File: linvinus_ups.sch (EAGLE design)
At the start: 19 parts, among them J1 BATTERY_CONNDEANS, Q1 IRF7240PBF, Q2 IRF7240PBF, Q3 BSS123, Q4 IRF7240PBF

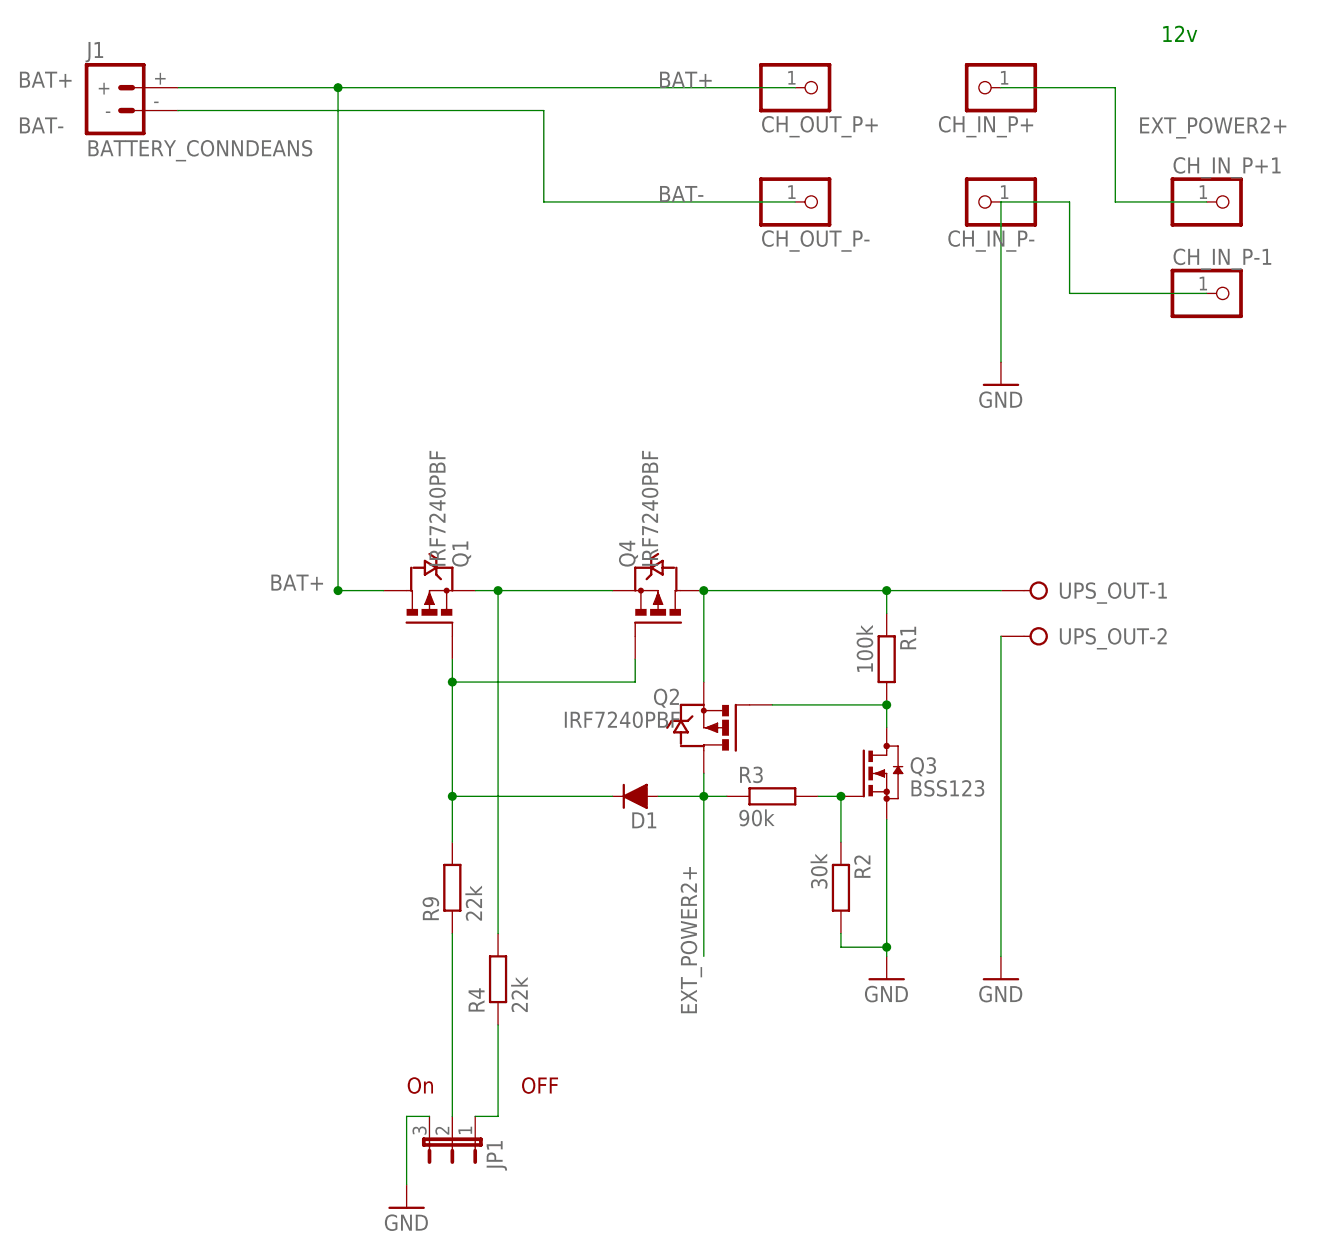
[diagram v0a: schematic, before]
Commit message: fix, completely close Q4 if vbatt > external power
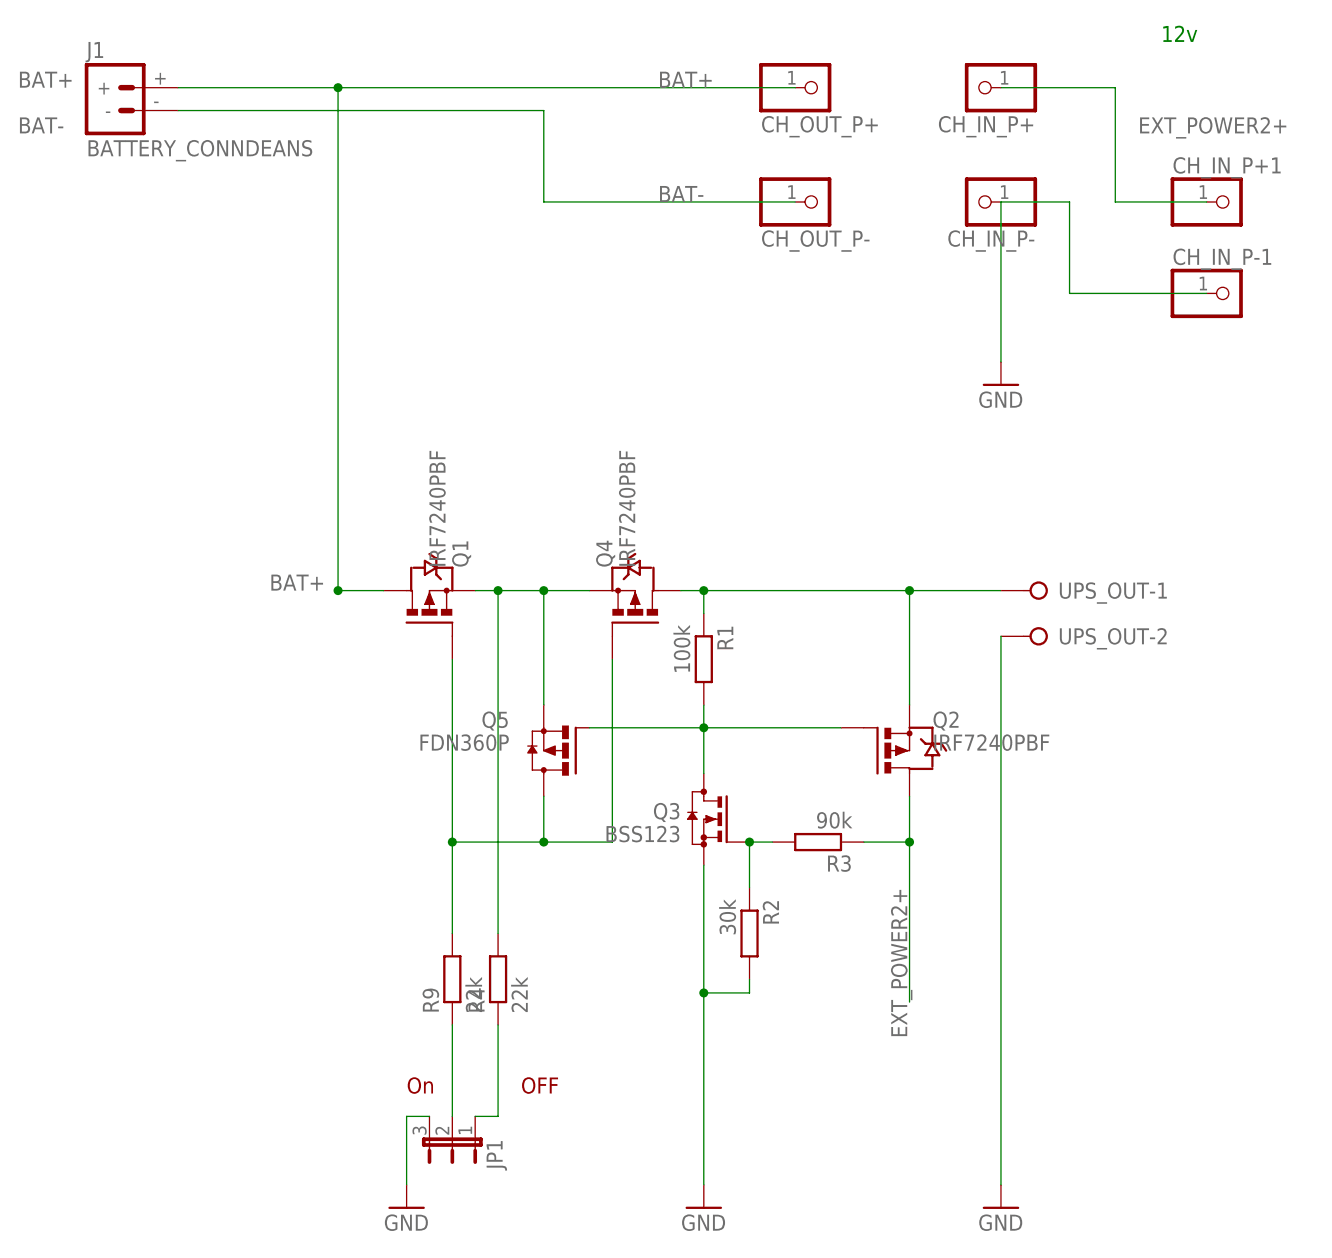
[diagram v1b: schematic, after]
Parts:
- removed D1: (no value), semicon-smd-ipc:D-FILL-SOD-80
- added Q5: FDN360P, transistor-power:FDN360P
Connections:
- net EXT_POWER2+: no longer D1.A
- net N$1: now also Q5.G
- net N$10: now also Q5.D; no longer D1.C
- net N$5: now also Q5.S
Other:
- moved on the sheet: Q2, Q3, Q4, R1, R2, R3, R9
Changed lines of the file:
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@@
 <part name="CH_IN_P-1" library="pinhead" deviceset="PINHD-1X1" device=""/>
 <part name="Q4" library="transistor-power" deviceset="P-MOSFET-SO8" device="" value="IRF7240PBF"/>
-<part name="D1" library="semicon-smd-ipc" deviceset="D-FILL-" device="SOD-80"/>
 <part name="R4" library="resistor" deviceset="R-EU_" device="R0805" value="22k"/>
 <part name="JP1" library="jumper" deviceset="JP2E" device=""/>
+<part name="Q5" library="transistor-power" deviceset="FDN360P" device=""/>
 </parts>
 <sheets>
@@
 <instance part="GND1" gate="1" x="124.46" y="66.04"/>
 <instance part="GND3" gate="1" x="58.42" y="-25.4"/>
-<instance part="R9" gate="G$1" x="63.5" y="10.16" rot="R90"/>
-<instance part="GND7" gate="1" x="124.46" y="0"/>
-<instance part="Q2" gate="G$1" x="93.98" y="27.94" rot="MR0"/>
-<instance part="Q3" gate="G$1" x="111.76" y="22.86"/>
-<instance part="R1" gate="G$1" x="111.76" y="35.56" rot="R270"/>
-<instance part="R2" gate="G$1" x="106.68" y="10.16" rot="R270"/>
-<instance part="R3" gate="G$1" x="99.06" y="20.32"/>
-<instance part="GND2" gate="1" x="111.76" y="0"/>
+<instance part="R9" gate="G$1" x="63.5" y="0" rot="R90"/>
+<instance part="GND7" gate="1" x="124.46" y="-25.4"/>
+<instance part="Q2" gate="G$1" x="111.76" y="25.4"/>
+<instance part="Q3" gate="G$1" x="91.44" y="17.78" rot="MR0"/>
+<instance part="R1" gate="G$1" x="91.44" y="35.56" rot="R270"/>
+<instance part="R2" gate="G$1" x="96.52" y="5.08" rot="R270"/>
+<instance part="R3" gate="G$1" x="104.14" y="15.24" rot="R180"/>
+<instance part="GND2" gate="1" x="91.44" y="-25.4"/>
 <instance part="J1" gate="G$1" x="25.4" y="99.06"/>
 <instance part="CH_IN_P+1" gate="G$1" x="149.86" y="86.36"/>
 <instance part="CH_IN_P-1" gate="G$1" x="149.86" y="76.2"/>
-<instance part="Q4" gate="G$1" x="86.36" y="40.64" rot="R90"/>
-<instance part="D1" gate="G$1" x="83.82" y="20.32" rot="R180"/>
+<instance part="Q4" gate="G$1" x="83.82" y="40.64" rot="R90"/>
 <instance part="R4" gate="G$1" x="68.58" y="0" rot="R90"/>
 <instance part="JP1" gate="1" x="63.5" y="-17.78" rot="R180"/>
+<instance part="Q5" gate="G$1" x="76.2" y="25.4" rot="MR0"/>
 </instances>
 <busses>
@@
 <net name="EXT_POWER2+" class="0">
 <segment>
-<label x="88.9" y="12.7" size="1.778" layer="95" rot="R270"/>
-<wire x1="91.44" y1="20.32" x2="91.44" y2="2.54" width="0.1524" layer="91"/>
+<label x="112.268" y="10.16" size="1.778" layer="95" rot="R270"/>
+<wire x1="114.3" y1="20.32" x2="114.3" y2="15.24" width="0.1524" layer="91"/>
 <pinref part="Q2" gate="G$1" pin="D"/>
-<wire x1="91.44" y1="20.32" x2="91.44" y2="22.86" width="0.1524" layer="91"/>
-<junction x="91.44" y="20.32"/>
 <pinref part="R3" gate="G$1" pin="1"/>
-<wire x1="91.44" y1="20.32" x2="93.98" y2="20.32" width="0.1524" layer="91"/>
-<pinref part="D1" gate="G$1" pin="A"/>
-<wire x1="86.36" y1="20.32" x2="91.44" y2="20.32" width="0.1524" layer="91"/>
+<wire x1="114.3" y1="15.24" x2="114.3" y2="-2.54" width="0.1524" layer="91"/>
+<wire x1="109.22" y1="15.24" x2="114.3" y2="15.24" width="0.1524" layer="91"/>
+<junction x="114.3" y="15.24"/>
 </segment>
 <segment>
@@
 <segment>
 <pinref part="UPS_OUT" gate="-2" pin="KL"/>
-<wire x1="124.46" y1="38.1" x2="124.46" y2="2.54" width="0.1524" layer="91"/>
+<wire x1="124.46" y1="38.1" x2="124.46" y2="-22.86" width="0.1524" layer="91"/>
 <pinref part="GND7" gate="1" pin="GND"/>
 </segment>
@@
 <pinref part="Q3" gate="G$1" pin="S"/>
 <pinref part="GND2" gate="1" pin="GND"/>
-<wire x1="111.76" y1="17.78" x2="111.76" y2="4.064" width="0.1524" layer="91"/>
+<wire x1="91.44" y1="12.7" x2="91.44" y2="-1.524" width="0.1524" layer="91"/>
 <pinref part="R2" gate="G$1" pin="2"/>
-<wire x1="111.76" y1="3.556" x2="111.76" y2="2.54" width="0.1524" layer="91"/>
-<wire x1="106.68" y1="5.08" x2="106.68" y2="3.556" width="0.1524" layer="91"/>
-<wire x1="106.68" y1="3.556" x2="111.76" y2="3.556" width="0.1524" layer="91"/>
-<wire x1="111.76" y1="3.556" x2="111.76" y2="4.064" width="0.1524" layer="91"/>
-<junction x="111.76" y="3.556"/>
+<wire x1="91.44" y1="-1.524" x2="91.44" y2="-22.86" width="0.1524" layer="91"/>
+<wire x1="96.52" y1="0" x2="96.52" y2="-1.524" width="0.1524" layer="91"/>
+<wire x1="96.52" y1="-1.524" x2="91.44" y2="-1.524" width="0.1524" layer="91"/>
+<junction x="91.44" y="-1.524"/>
 </segment>
 <segment>
@@
 </segment>
 </net>
-<net name="N$6" class="0">
-<segment>
-<pinref part="UPS_OUT" gate="-1" pin="KL"/>
-<wire x1="124.46" y1="43.18" x2="111.76" y2="43.18" width="0.1524" layer="91"/>
-<pinref part="Q2" gate="G$1" pin="S"/>
-<wire x1="111.76" y1="43.18" x2="91.44" y2="43.18" width="0.1524" layer="91"/>
-<wire x1="91.44" y1="33.02" x2="91.44" y2="43.18" width="0.1524" layer="91"/>
-<pinref part="R1" gate="G$1" pin="1"/>
-<wire x1="111.76" y1="40.64" x2="111.76" y2="43.18" width="0.1524" layer="91"/>
-<junction x="111.76" y="43.18"/>
-<pinref part="Q4" gate="G$1" pin="D"/>
-<junction x="91.44" y="43.18"/>
-</segment>
-</net>
 <net name="N$10" class="0">
 <segment>
 <pinref part="Q1" gate="G$1" pin="G"/>
 <pinref part="R9" gate="G$1" pin="2"/>
-<wire x1="63.5" y1="15.24" x2="63.5" y2="20.32" width="0.1524" layer="91"/>
-<wire x1="63.5" y1="20.32" x2="63.5" y2="33.02" width="0.1524" layer="91"/>
-<wire x1="63.5" y1="33.02" x2="63.5" y2="35.56" width="0.1524" layer="91"/>
+<wire x1="63.5" y1="5.08" x2="63.5" y2="15.24" width="0.1524" layer="91"/>
+<wire x1="63.5" y1="15.24" x2="63.5" y2="35.56" width="0.1524" layer="91"/>
 <pinref part="Q4" gate="G$1" pin="G"/>
-<wire x1="83.82" y1="35.56" x2="83.82" y2="33.02" width="0.1524" layer="91"/>
-<wire x1="83.82" y1="33.02" x2="63.5" y2="33.02" width="0.1524" layer="91"/>
-<junction x="63.5" y="33.02"/>
-<pinref part="D1" gate="G$1" pin="C"/>
-<wire x1="81.28" y1="20.32" x2="63.5" y2="20.32" width="0.1524" layer="91"/>
-<junction x="63.5" y="20.32"/>
+<wire x1="81.28" y1="35.56" x2="81.28" y2="15.24" width="0.1524" layer="91"/>
+<wire x1="81.28" y1="15.24" x2="73.66" y2="15.24" width="0.1524" layer="91"/>
+<junction x="63.5" y="15.24"/>
+<wire x1="73.66" y1="15.24" x2="63.5" y2="15.24" width="0.1524" layer="91"/>
+<pinref part="Q5" gate="G$1" pin="D"/>
+<wire x1="73.66" y1="20.32" x2="73.66" y2="15.24" width="0.1524" layer="91"/>
+<junction x="73.66" y="15.24"/>
 </segment>
 </net>
@@
 <net name="N$1" class="0">
 <segment>
+<pinref part="R1" gate="G$1" pin="2"/>
+<pinref part="Q3" gate="G$1" pin="D"/>
+<wire x1="91.44" y1="30.48" x2="91.44" y2="27.94" width="0.1524" layer="91"/>
+<pinref part="Q5" gate="G$1" pin="G"/>
+<wire x1="91.44" y1="27.94" x2="91.44" y2="22.86" width="0.1524" layer="91"/>
+<wire x1="78.74" y1="27.94" x2="91.44" y2="27.94" width="0.1524" layer="91"/>
+<junction x="91.44" y="27.94"/>
 <pinref part="Q2" gate="G$1" pin="G"/>
-<pinref part="R1" gate="G$1" pin="2"/>
-<wire x1="99.06" y1="30.48" x2="111.76" y2="30.48" width="0.1524" layer="91"/>
-<pinref part="Q3" gate="G$1" pin="D"/>
-<wire x1="111.76" y1="30.48" x2="111.76" y2="27.94" width="0.1524" layer="91"/>
-<junction x="111.76" y="30.48"/>
+<wire x1="106.68" y1="27.94" x2="91.44" y2="27.94" width="0.1524" layer="91"/>
 </segment>
 </net>
@@
 <pinref part="R3" gate="G$1" pin="2"/>
 <pinref part="Q3" gate="G$1" pin="G"/>
-<wire x1="104.14" y1="20.32" x2="106.68" y2="20.32" width="0.1524" layer="91"/>
+<wire x1="99.06" y1="15.24" x2="96.52" y2="15.24" width="0.1524" layer="91"/>
 <pinref part="R2" gate="G$1" pin="1"/>
-<wire x1="106.68" y1="15.24" x2="106.68" y2="20.32" width="0.1524" layer="91"/>
-<junction x="106.68" y="20.32"/>
+<wire x1="96.52" y1="10.16" x2="96.52" y2="15.24" width="0.1524" layer="91"/>
+<junction x="96.52" y="15.24"/>
 </segment>
 </net>
@@
 <wire x1="66.04" y1="43.18" x2="68.58" y2="43.18" width="0.1524" layer="91"/>
 <pinref part="R4" gate="G$1" pin="2"/>
-<wire x1="68.58" y1="43.18" x2="81.28" y2="43.18" width="0.1524" layer="91"/>
+<wire x1="68.58" y1="43.18" x2="73.66" y2="43.18" width="0.1524" layer="91"/>
+<wire x1="73.66" y1="43.18" x2="78.74" y2="43.18" width="0.1524" layer="91"/>
 <wire x1="68.58" y1="5.08" x2="68.58" y2="43.18" width="0.1524" layer="91"/>
 <junction x="68.58" y="43.18"/>
+<pinref part="Q5" gate="G$1" pin="S"/>
+<wire x1="73.66" y1="30.48" x2="73.66" y2="43.18" width="0.1524" layer="91"/>
+<junction x="73.66" y="43.18"/>
 </segment>
 </net>
@@
 <pinref part="JP1" gate="1" pin="2"/>
 <pinref part="R9" gate="G$1" pin="1"/>
-<wire x1="63.5" y1="-15.24" x2="63.5" y2="5.08" width="0.1524" layer="91"/>
+<wire x1="63.5" y1="-15.24" x2="63.5" y2="-5.08" width="0.1524" layer="91"/>
 </segment>
 </net>
@@
 </segment>
 </net>
+<net name="N$6" class="0">
+<segment>
+<pinref part="Q4" gate="G$1" pin="D"/>
+<pinref part="UPS_OUT" gate="-1" pin="KL"/>
+<wire x1="88.9" y1="43.18" x2="91.44" y2="43.18" width="0.1524" layer="91"/>
+<pinref part="R1" gate="G$1" pin="1"/>
+<wire x1="91.44" y1="43.18" x2="114.3" y2="43.18" width="0.1524" layer="91"/>
+<wire x1="114.3" y1="43.18" x2="124.46" y2="43.18" width="0.1524" layer="91"/>
+<wire x1="91.44" y1="40.64" x2="91.44" y2="43.18" width="0.1524" layer="91"/>
+<pinref part="Q2" gate="G$1" pin="S"/>
+<wire x1="114.3" y1="30.48" x2="114.3" y2="43.18" width="0.1524" layer="91"/>
+<junction x="114.3" y="43.18"/>
+<junction x="91.44" y="43.18"/>
+</segment>
+</net>
